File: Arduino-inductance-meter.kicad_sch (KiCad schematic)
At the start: 5 parts, among them J1 Conn_01x05_Pin, U1 NE555P, U2 NE555P

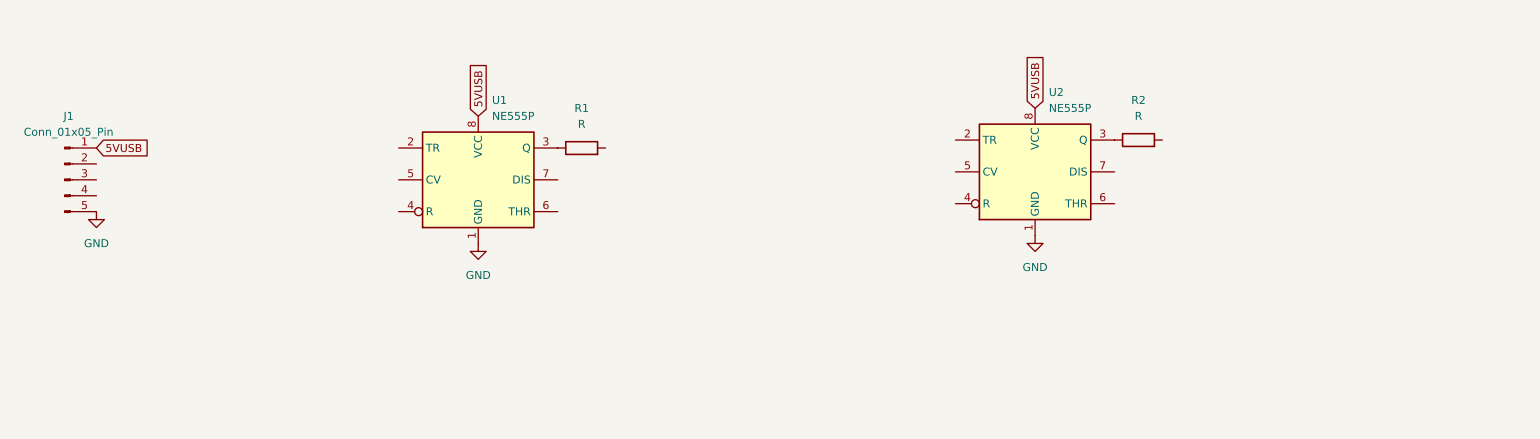
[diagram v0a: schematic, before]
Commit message: finished layout, not verified
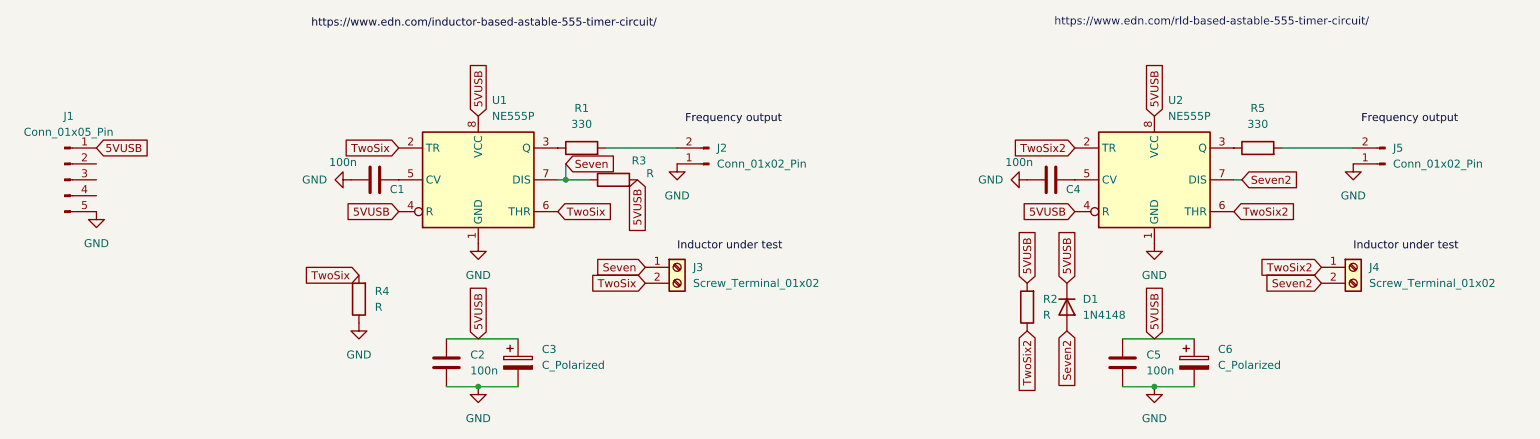
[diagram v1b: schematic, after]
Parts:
- added C1, C2, C4, C5: 100n, Capacitor_SMD:C_0805_2012Metric, symbol Device:C
- added C3, C6: C_Polarized, Capacitor_THT:CP_Radial_D5.0mm_P2.50mm, symbol Device:C_Polarized
- added D1: 1N4148, Diode_THT:D_DO-35_SOD27_P7.62mm_Horizontal, symbol Diode:1N4148
- added J2, J5: Conn_01x02_Pin, Connector_PinHeader_2.54mm:PinHeader_1x02_P2.54mm_Vertical, symbol Connector:Conn_01x02_Pin
- added J3, J4: Screw_Terminal_01x02, TerminalBlock_Phoenix:TerminalBlock_Phoenix_MKDS-3-2-5.08_1x02_P5.08mm_Horizontal, symbol Connector:Screw_Terminal_01x02
- added R3, R4: R, Resistor_THT:R_Axial_DIN0411_L9.9mm_D3.6mm_P12.70mm_Horizontal, symbol Device:R
- added R5: 330, Resistor_SMD:R_0805_2012Metric, symbol Device:R
- J1: footprint (none) -> Connector_PinHeader_2.54mm:PinHeader_1x05_P2.54mm_Vertical
- R1: value R -> 330; footprint (none) -> Resistor_SMD:R_0805_2012Metric
- R2: footprint (none) -> Resistor_THT:R_Axial_DIN0411_L9.9mm_D3.6mm_P12.70mm_Horizontal
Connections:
- net 5VUSB: now also R2.2, U1.4 (R), U2.4 (R), C2.2, C3.1, C5.2, C6.1, D1.1 (K), R3.2
- net GND: now also C1.1, C2.1, C3.2, C4.1, C5.1, C6.2, J2.1 (Pin_1), J5.1 (Pin_1), R4.1
- net at U2.3 (Q): now also R5.1; no longer R2.1
- net TwoSix: now reaches U1.2 (TR)
- net TwoSix: now also U1.6 (THR), J3.2 (Pin_2), R4.2
- net at U1.5 (CV): now also C1.2
- net Seven: now reaches U1.7 (DIS)
- net Seven: now also J3.1 (Pin_1), R3.1
- net at R1.2: now also J2.2 (Pin_2)
- net TwoSix2: now reaches U2.2 (TR)
- net TwoSix2: now also R2.1, U2.6 (THR), J4.1 (Pin_1)
- net at U2.5 (CV): now also C4.2
- net Seven2: now reaches U2.7 (DIS)
- net Seven2: now also D1.2 (A), J4.2 (Pin_2)
- new net: J5.2 (Pin_2), R5.2
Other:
- note added: "https://www.edn.com/rld-based-astable-555-timer-circuit/"
